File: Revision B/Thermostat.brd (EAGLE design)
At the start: 50.5 x 52.1 mm, 22 parts, among them K1 G5LE, K2 G5LE, K3 G5LE

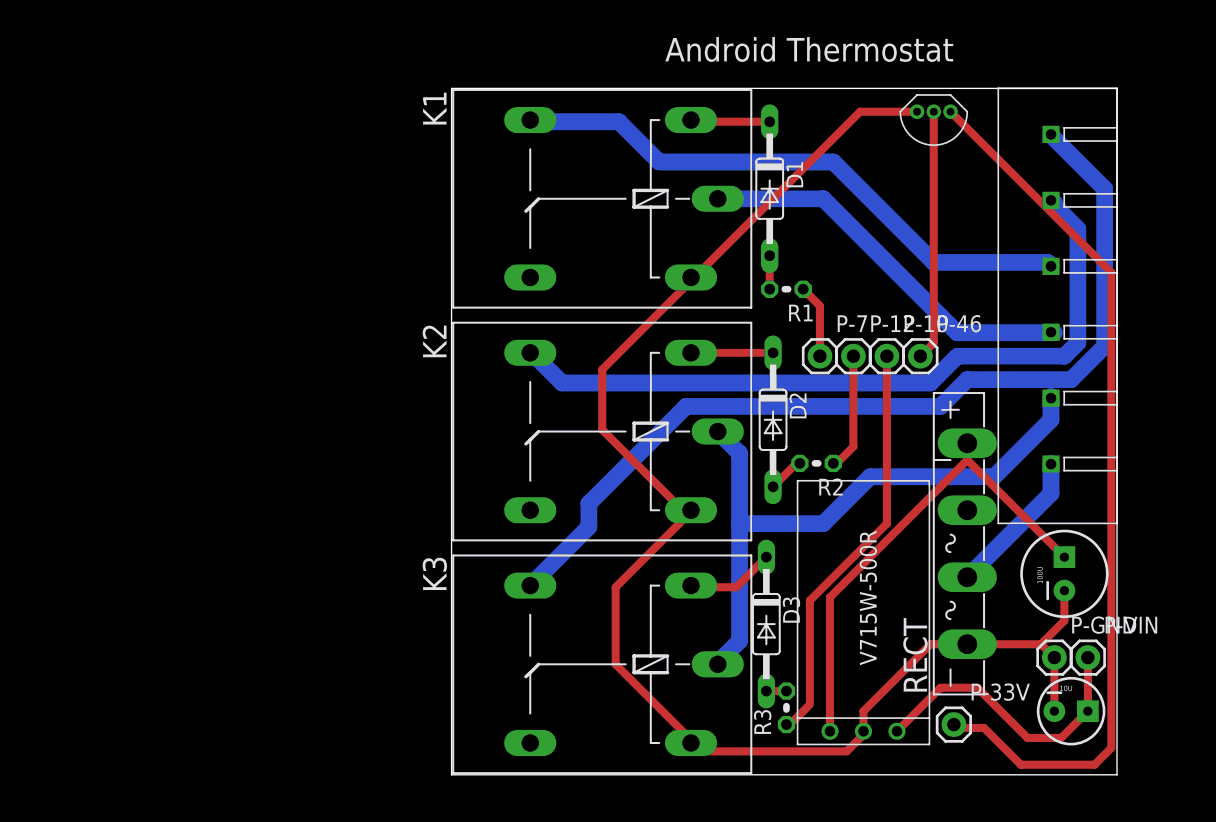
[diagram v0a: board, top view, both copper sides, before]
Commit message: Added Transistors
The IOIO can only supply 20ma from the digital pins, so I added
transistors to feed 5v and switched to the 5v relays.
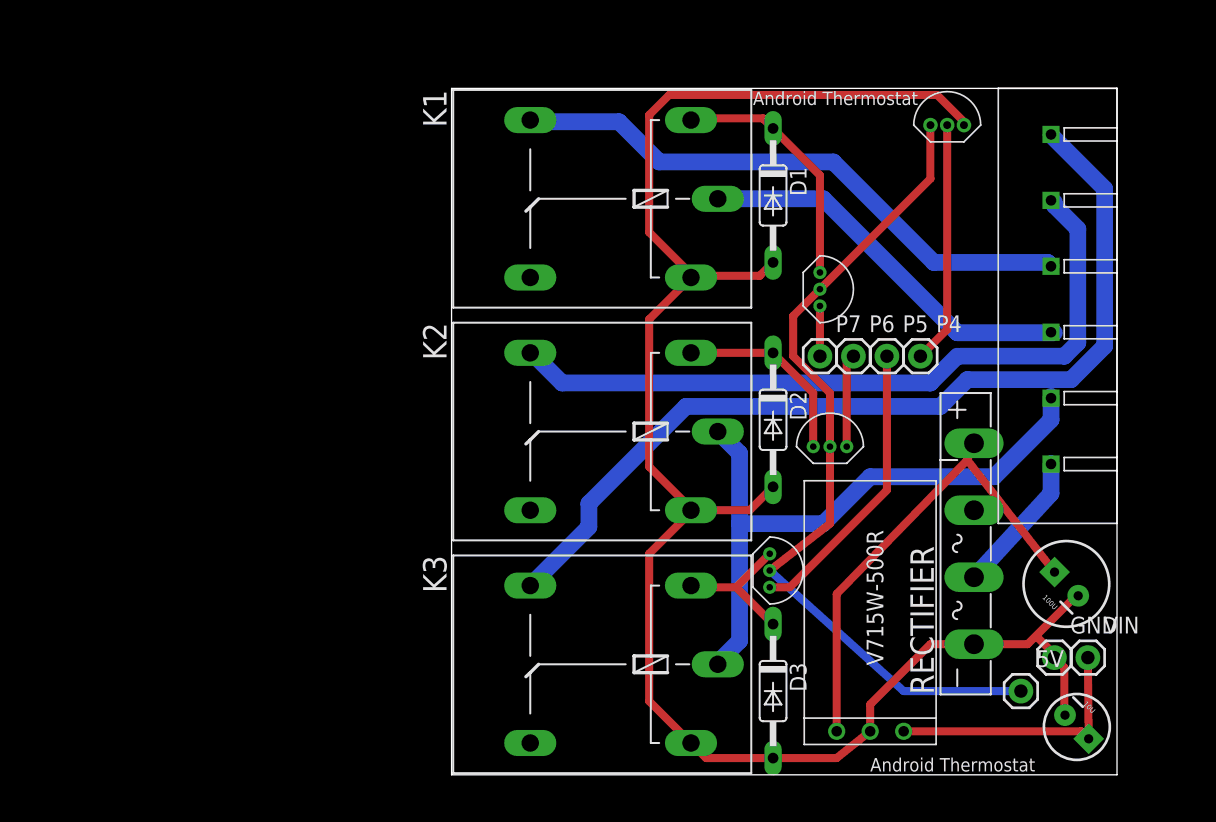
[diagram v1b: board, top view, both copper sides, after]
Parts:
- removed P-33V: M01PTH, SparkFun-Connectors:1X01
- removed R1, R2, R3: (no value), resistor:0204V
- removed RECT: (no value), rectifier:GBU4S
- added 5V: (no value), SparkFun-Connectors:1X01
- added RECTIFIER: (no value), rectifier:GBU4S
- added U$4, U$5, U$6: TRANSISTOR, android-thermostat:TRANSISTOR
- GND, P4, P5, P6, P7, VIN: value M01PTH -> (none)
- K1, K2, K3: value G5LE -> (none)
- moved D3 5.11 mm to (49.8, 6.35)
- moved U$1 1.44 mm to (63.0, 49.3), turned to 90 degrees
- moved 10U 1.27 mm to (72.8, 3.63), turned to 315 degrees
- moved 100U 0.78 mm to (72.0, 14.5), turned to 135 degrees
- moved D1 0.57 mm to (49.8, 43.9)
- moved U$2 0.51 mm to (57.1, 3.30)
- renumbered P-10 to P5, P-12 to P6, P-46 to P4, P-7 to P7, P-GND to GND, P-VIN to VIN
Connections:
- removed net GND: 100U.2, 10U.2, GND.1, K1.2, K2.2, K3.2, RECT.-, U$1.GND-3, U$2.GND
- removed net N$17: P7.1, R1.1
- removed net N$27: P6.1, R2.1
- removed net N$4 (its old number): D3.C, K3.1
- removed net N$9: D1.C, K1.1
- new net +5V: 5V.1, U$1.VCC-1, U$4.C, U$5.C, U$6.C
- new net N$11: D2.C, K2.1, U$5.E
- net N$10: now also RECTIFIER.+; no longer RECT.+
- net N$16: now also D3.C, K3.1, U$6.E; no longer D1.A, R1.2
- net N$2: now also 10U.2, D1.A, D2.A, D3.A, GND.1, K1.2, K2.2, K3.2, RECTIFIER.-, U$1.GND-3, U$2.GND; no longer P5.1, R3.1
- net N$20: now also RECTIFIER.AC2; no longer RECT.AC2
- net N$24: now also RECTIFIER.AC1; no longer RECT.AC1
- net N$3: now also P7.1, U$4.B; no longer D3.A, R3.2
- net N$6: now also P6.1, U$5.B; no longer D2.C, K2.1
- net N$7: now also P5.1, U$6.B; no longer D2.A, R2.2
- net N$8: now also D1.C, K1.1, U$4.E; no longer P-33V.1, U$1.VCC-1
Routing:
- net GND: track 109.5 -> 0.00 mm
- net N$2: track 28.6 -> 133.9 mm
- net +5V: track 0.00 -> 64.0 mm
- net N$8: track 66.7 -> 18.6 mm
- net N$7: track 2.77 -> 21.8 mm
- net N$11: track 0.00 -> 14.5 mm
- net N$27: track 8.91 -> 0.00 mm
- net N$16: track 2.54 -> 10.8 mm
- net N$4 (its old number): track 6.53 -> 0.00 mm
- net N$17: track 5.61 -> 0.00 mm
- net N$9: track 5.84 -> 2.16 mm
- net N$26: track 2.41 -> 0.00 mm
- net N$3: track 1.52 -> 3.81 mm
- net N$18: track 22.3 -> 20.4 mm
- net N$6: track 6.10 -> 6.81 mm
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
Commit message: Finished Board Layout with Transistors
Changed the transistor symbol.
Changed wires to routes
Verified against design rules
Added top and bottom silk text
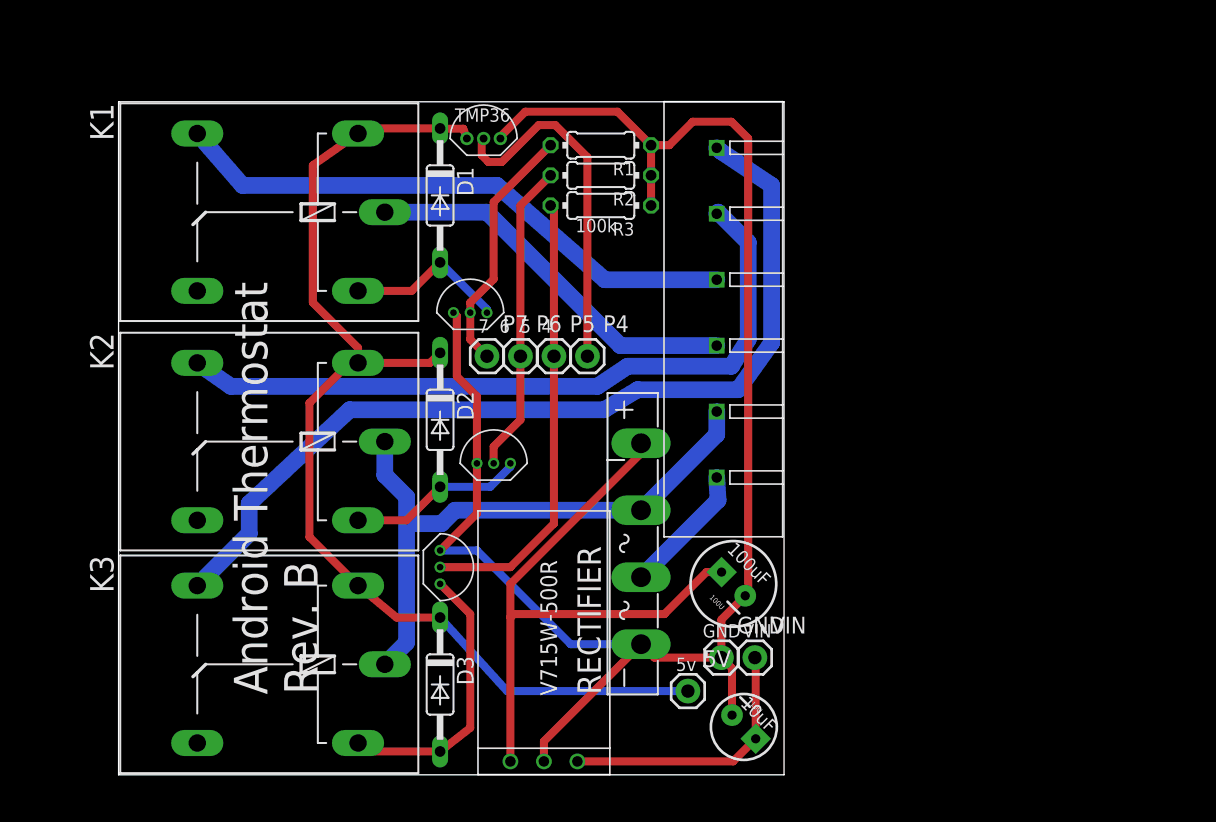
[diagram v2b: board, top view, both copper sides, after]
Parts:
- removed U$4, U$5, U$6: TRANSISTOR, android-thermostat:TRANSISTOR
- added R1, R2, R3: (no value), rcl:0204/7
- added T1, T2, T3: MOSFET, android-thermostat:TRANSISTOR
- moved U$1 35.2 mm to (27.8, 48.3)
- moved U$3 25.4 mm to (45.5, 35.1)
- moved K1 25.3 mm to (10.8, 42.7)
- moved K2 25.3 mm to (10.8, 25.3)
- moved D3 25.3 mm to (24.5, 6.85)
- moved 10U 25.3 mm to (47.6, 3.63)
- moved GND 25.3 mm to (45.9, 8.89)
- moved P5 25.3 mm to (33.2, 31.8)
- moved P7 25.3 mm to (28.1, 31.8)
- moved P6 25.3 mm to (30.6, 31.8)
- moved 100U 25.3 mm to (46.8, 14.5)
- moved 5V 25.3 mm to (43.3, 6.35)
- moved D1 25.3 mm to (24.5, 43.9)
- moved D2 25.3 mm to (24.5, 26.9)
- moved K3 25.3 mm to (10.8, 8.38)
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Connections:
- removed net N$11: D2.C, K2.1, U$5.E
- removed net N$8 (its old number): D1.C, K1.1, U$4.E
- new net GND: 100U.2, 10U.2, GND.1, R1.1, R2.1, R3.1, RECTIFIER.-, T1.S, T2.S, T3.S, U$1.GND-3, U$2.GND
- new net N$17: P5.1, R3.2, T3.G
- new net N$18: D3.A, K3.2, T3.D
- net +5V: now also D1.C, D2.C, D3.C, K1.1, K2.1, K3.1; no longer 5V.1, U$1.VCC-1, U$4.C, U$5.C, U$6.C
- net N$16: now also 5V.1, U$1.VCC-1; no longer D3.C, K3.1, U$6.E
- net N$2: now also P6.1, R2.2, T2.G; no longer 10U.2, D1.A, D2.A, D3.A, GND.1, K1.2, K2.2, K3.2, RECTIFIER.-, U$1.GND-3, U$2.GND
- net N$3: now also D2.A, K2.2, T2.D; no longer P7.1, U$4.B
- net N$6: now also P7.1, R1.2, T1.G; no longer P6.1, U$5.B
- net N$7: now also D1.A, K1.2, T1.D; no longer P5.1, U$6.B
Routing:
- net GND: track 0.00 -> 128.1 mm
- net N$2: track 133.9 -> 23.6 mm
- net N$23: track 69.6 -> 0.00 mm
- net N$13: track 0.00 -> 69.5 mm
- net N$15: track 0.00 -> 54.7 mm
- net N$12: track 47.9 -> 0.00 mm
- net N$8: track 0.00 -> 46.4 mm
- net N$14: track 0.00 -> 43.9 mm
- net N$19: track 43.6 -> 0.00 mm
- net N$17: track 0.00 -> 34.2 mm
- net N$22: track 34.0 -> 0.00 mm
- net N$1: track 0.00 -> 29.4 mm
- net N$5: track 29.4 -> 0.00 mm
- net N$18: track 0.00 -> 21.0 mm
- net N$21: track 20.7 -> 0.00 mm
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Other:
- board size 50.5 x 52.1 mm -> 50.5 x 51 mm
- board text added: "100k"
- board text added: "100uF"
- board text added: "10uF"
- board text added: "5v"
- board text added: "7 6 5 4"
- board text added: "C"
- board text added: "G"
- board text added: "GND"
- board text added: "RC"
- board text added: "RH"
- board text added: "Rev. B"
- board text added: "TMP36"
- board text added: "VIN"
- board text added: "W"
- board text added: "Y"

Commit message: First Test Print
Added Labels
Exported Gerber Files
Ordered Test Print
Adjusted borders to exact 2"x2" after ordering the print.
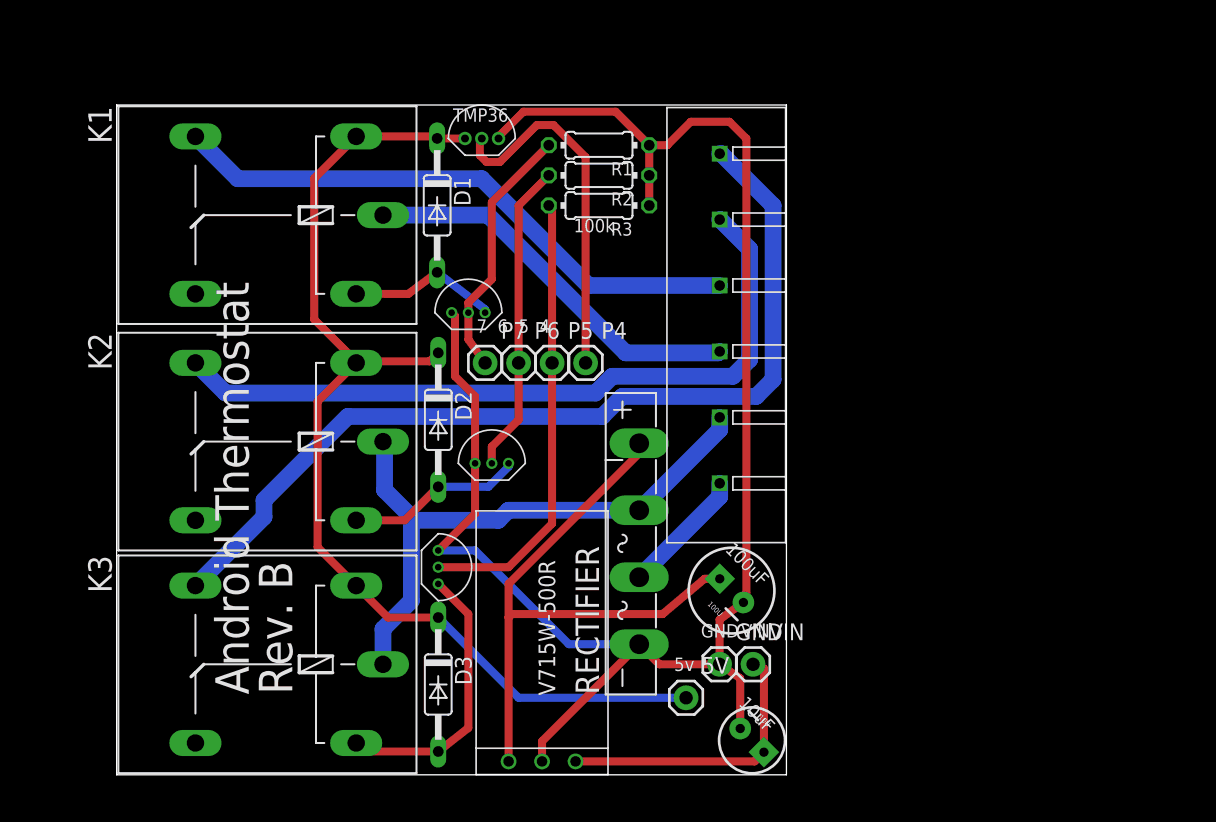
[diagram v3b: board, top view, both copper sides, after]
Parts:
- moved 10U 1.19 mm to (48.2, 2.61)
- moved D1 0.79 mm to (24.3, 43.2)
- moved P4 0.53 mm to (35.6, 31.2)
- moved GND 0.53 mm to (45.7, 8.38)
- moved VIN 0.53 mm to (48.3, 8.38)
- moved P6 0.53 mm to (30.5, 31.2)
- moved 5V 0.53 mm to (43.2, 5.84)
- moved 100U 0.53 mm to (46.6, 14.0)
- moved P5 0.53 mm to (33.0, 31.2)
- moved P7 0.53 mm to (27.9, 31.2)
- moved U$3 0.50 mm to (45.7, 34.6)
- moved K1 0.26 mm to (10.7, 42.4)
- moved R1 0.14 mm to (36.6, 47.8)
- moved R2 0.14 mm to (36.6, 45.5)
- moved R3 0.14 mm to (36.6, 43.2)
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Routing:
- net +5V: track 61.8 -> 59.0 mm
- net GND: track 128.1 -> 129.9 mm
- net N$10: track 20.4 -> 21.8 mm
- net N$15: track 54.7 -> 55.6 mm
- net N$7: track 12.4 -> 11.5 mm
- net N$8: track 46.4 -> 45.8 mm
- net N$14: track 43.9 -> 44.4 mm
- net N$1: track 29.4 -> 29.9 mm
- net N$16: track 23.9 -> 23.4 mm
- net N$4: track 26.8 -> 27.3 mm
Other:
- board size 50.5 x 51 mm -> 50.8 x 50.8 mm

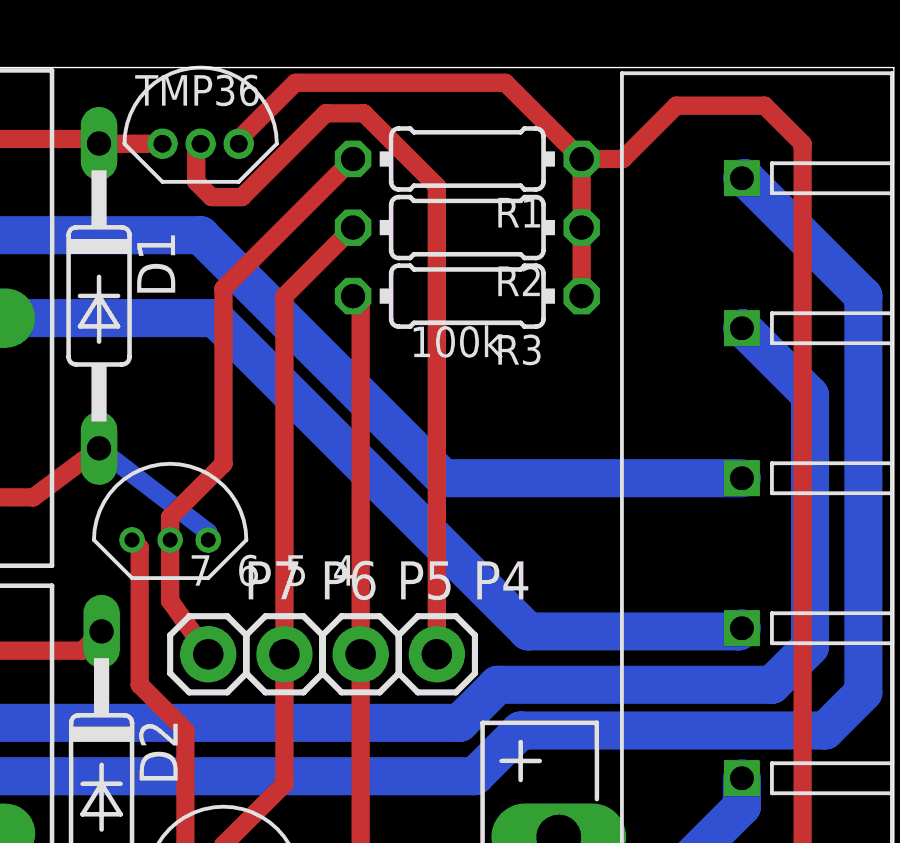
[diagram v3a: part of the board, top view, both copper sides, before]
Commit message: Added Temperature Sensor Capacitor
Added a capacitor to pin 4 to smooth out the voltage reading from the
temperature sensor.  I still need to calculate exactly what size that
capacitor should be.
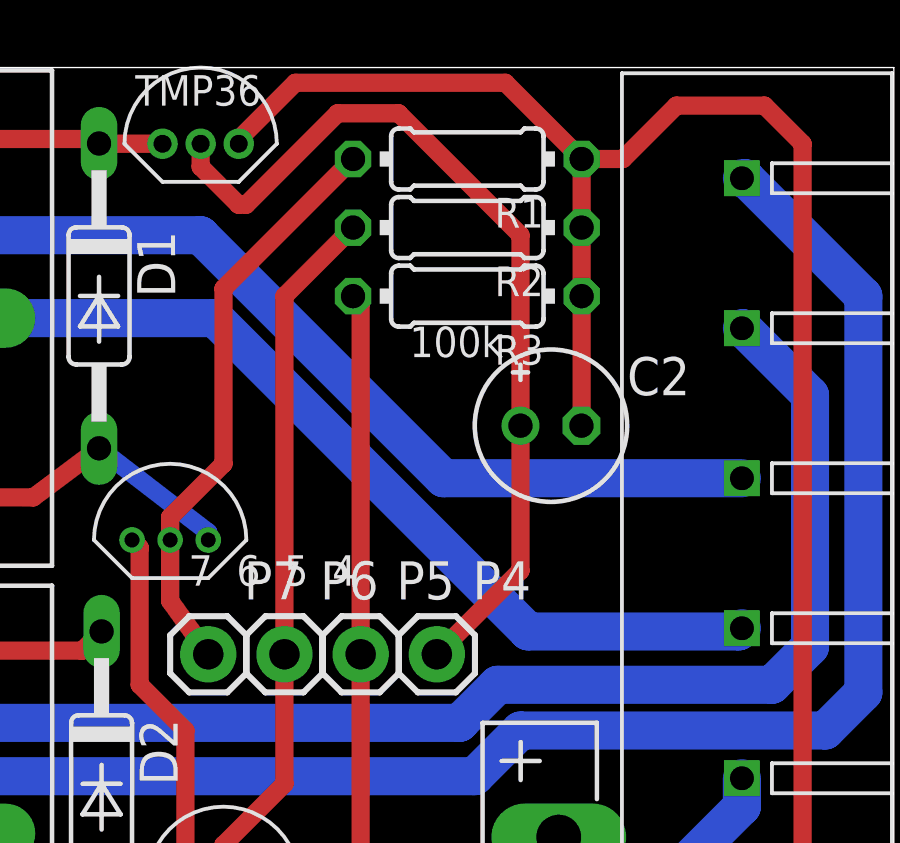
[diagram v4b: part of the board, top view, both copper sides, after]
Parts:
- added C2: (no value), rcl:E2-5
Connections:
- net GND: now also C2.-
- net N$4: now also C2.+
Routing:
- net GND: track 129.9 -> 134.3 mm
- net N$4: track 27.3 -> 30.0 mm
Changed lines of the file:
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@@
 <element name="T2" library="android-thermostat" package="TRANSISTOR" value="MOSFET" x="28.4543" y="23.622" rot="R90"/>
 <element name="T1" library="android-thermostat" package="TRANSISTOR" value="MOSFET" x="26.6763" y="35.052" rot="R90"/>
+<element name="C2" library="rcl" package="E2-5" value="" x="39.37" y="38.862"/>
 </elements>
 <signals>
@@
 <wire x1="45.7263" y1="8.382" x2="41.1543" y2="8.382" width="0.6096" layer="1"/>
 <wire x1="41.1543" y1="8.382" x2="39.6303" y2="9.906" width="0.6096" layer="1"/>
-</signal>
-<signal name="N$4">
-<contactref element="P4" pad="1"/>
-<contactref element="U$1" pad="DATA-2"/>
-<wire x1="35.5663" y1="31.242" x2="35.5663" y2="46.844" width="0.6096" layer="1"/>
-<wire x1="35.5663" y1="46.844" x2="33.1343" y2="49.276" width="0.6096" layer="1"/>
-<wire x1="33.1343" y1="49.276" x2="31.8643" y2="49.276" width="0.6096" layer="1"/>
-<wire x1="31.8643" y1="49.276" x2="29.0703" y2="46.482" width="0.6096" layer="1"/>
-<wire x1="29.0703" y1="46.482" x2="28.0543" y2="46.482" width="0.6096" layer="1"/>
-<wire x1="28.0543" y1="46.482" x2="27.5463" y2="46.99" width="0.6096" layer="1"/>
-<wire x1="27.5463" y1="46.99" x2="27.5463" y2="48.114" width="0.6096" layer="1"/>
-<wire x1="27.5463" y1="48.114" x2="27.6923" y2="48.26" width="0.6096" layer="1"/>
+<contactref element="C2" pad="-"/>
+<wire x1="40.3923" y1="43.18" x2="40.3923" y2="38.8683" width="0.6096" layer="1"/>
+<wire x1="40.3923" y1="38.8683" x2="40.386" y2="38.862" width="0.6096" layer="1"/>
 </signal>
 <signal name="N$8">
@@
 <wire x1="29.9783" y1="12.192" x2="29.7243" y2="11.938" width="0.6096" layer="1"/>
 </signal>
+<signal name="N$4">
+<contactref element="U$1" pad="DATA-2"/>
+<contactref element="C2" pad="+"/>
+<contactref element="P4" pad="1"/>
+<wire x1="27.6923" y1="48.26" x2="27.6923" y2="47.4917" width="0.6096" layer="1"/>
+<wire x1="27.6923" y1="47.4917" x2="28.956" y2="46.228" width="0.6096" layer="1"/>
+<wire x1="28.956" y1="46.228" x2="29.21" y2="46.228" width="0.6096" layer="1"/>
+<wire x1="29.21" y1="46.228" x2="32.258" y2="49.276" width="0.6096" layer="1"/>
+<wire x1="32.258" y1="49.276" x2="34.29" y2="49.276" width="0.6096" layer="1"/>
+<wire x1="34.29" y1="49.276" x2="38.354" y2="45.212" width="0.6096" layer="1"/>
+<wire x1="38.354" y1="45.212" x2="38.354" y2="38.862" width="0.6096" layer="1"/>
+<wire x1="38.354" y1="38.862" x2="38.354" y2="34.0297" width="0.6096" layer="1"/>
+<wire x1="38.354" y1="34.0297" x2="35.5663" y2="31.242" width="0.6096" layer="1"/>
+</signal>
 </signals>
